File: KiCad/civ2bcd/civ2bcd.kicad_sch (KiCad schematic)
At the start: 56 parts, among them J1 7-15VDC, J2 CI-V (OUT), J3 SWD, J4 BCD OUTPUT 1, J5 BCD OUTPUT 2, J6 CI-V (IN), Q1 BC817, Q2 BC817, Q3 BC817, Q4 BC817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

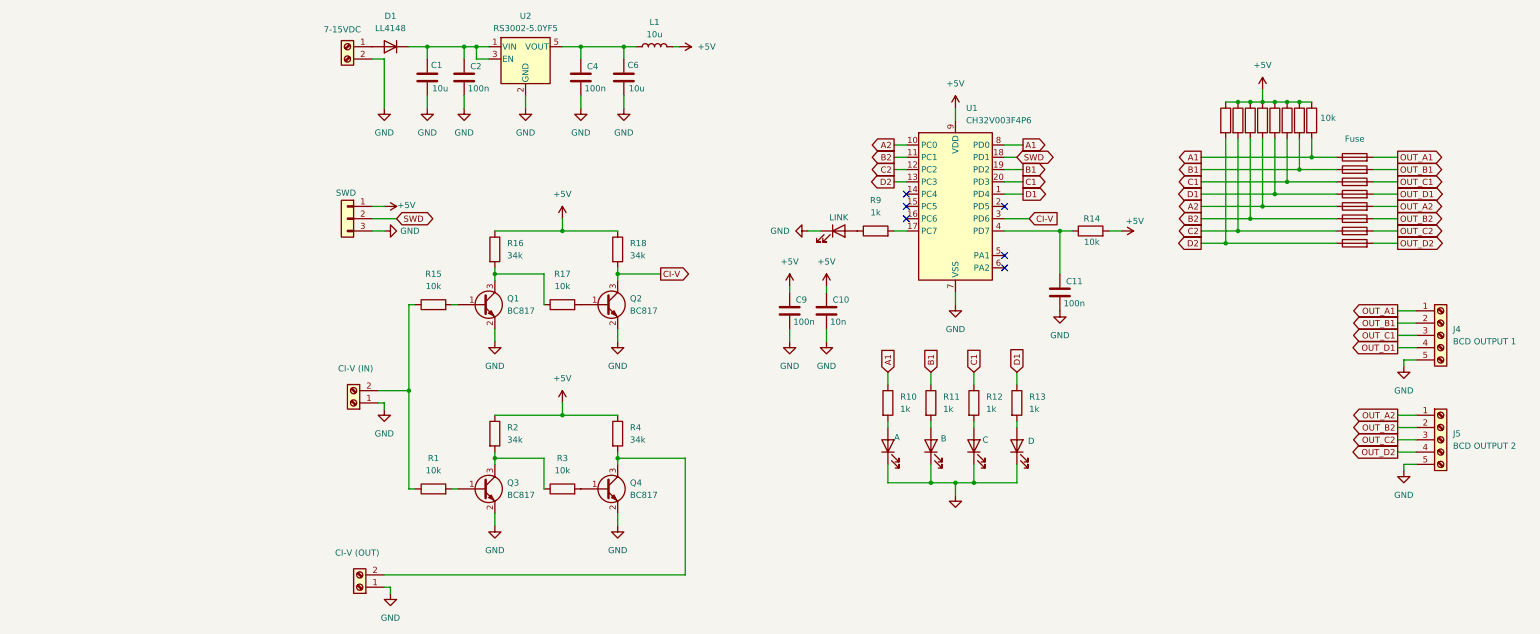
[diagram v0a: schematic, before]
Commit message: fix issues with civ input
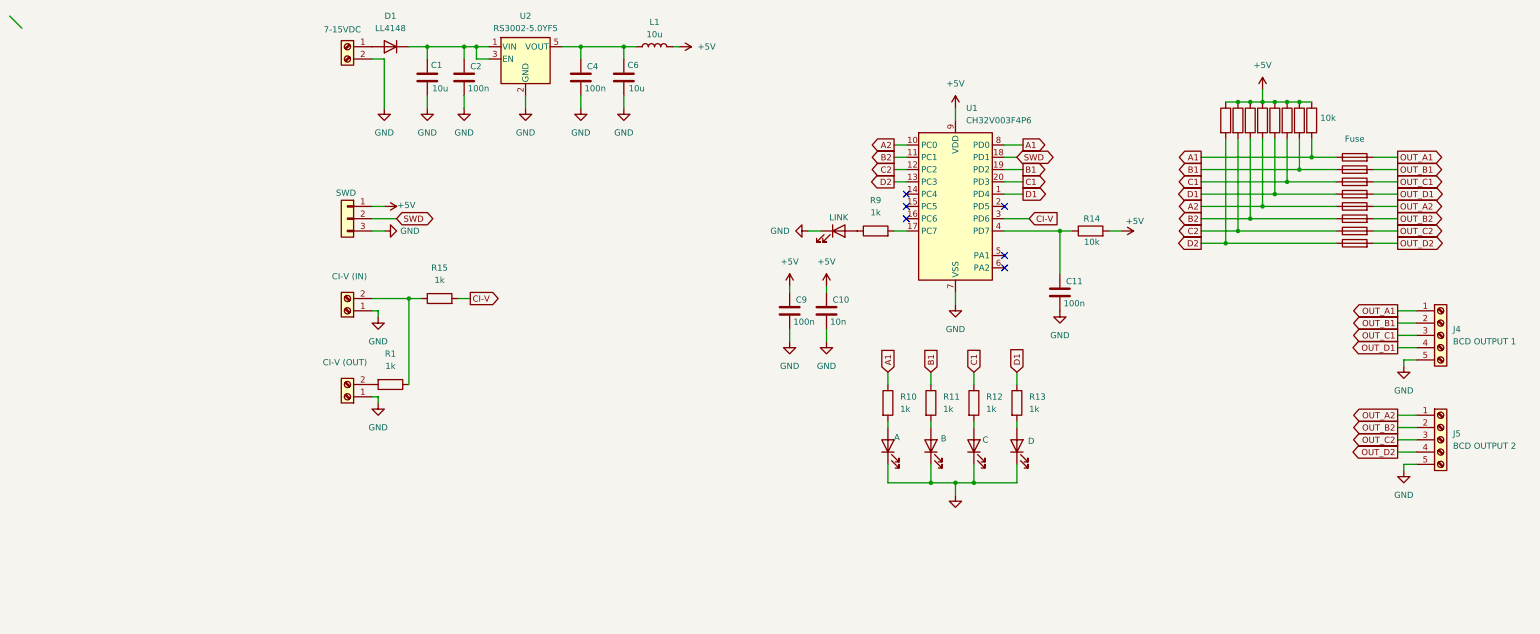
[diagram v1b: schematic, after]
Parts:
- removed Q1, Q2, Q3, Q4: BC817, Package_TO_SOT_SMD:SOT-23, symbol Transistor_BJT:BC817
- removed R16, R18, R2, R4: 34k, Resistor_SMD:R_1206_3216Metric, symbol Device:R
- removed R17, R3: 10k, Resistor_SMD:R_1206_3216Metric, symbol Device:R
- R1, R15: value 10k -> 1k
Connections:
- net CI-V: now also R15.2
- net at J2.2 (Pin_2): now also R1.2
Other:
- moved on the sheet: R1, R15

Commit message: fix civ connection
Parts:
- removed R1: 1k, Resistor_SMD:R_1206_3216Metric, symbol Device:R
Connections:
- net at J6.2 (Pin_2), R15.1: now also J2.2 (Pin_2)
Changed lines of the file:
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@@
 	(wire
 		(pts
+			(xy 34.29 104.14) (xy 41.91 104.14)
+		)
+		(stroke
+			(width 0)
+			(type default)
+		)
+	)
+	(wire
+		(pts
 			(xy 205.74 64.77) (xy 220.98 64.77)
 		)
@@
 					(unit 1)
 				)
-			)
-		)
-	)
-	(symbol
-		(lib_id "Device:R")
-		(at 38.1 104.14 270)
-		(unit 1)
-		(exclude_from_sim no)
-		(in_bom yes)
-		(on_board yes)
-		(dnp no)
-		(fields_autoplaced yes)
-		(property "Reference" "R1"
-			(at 38.1 97.79 90)
-			(effects
-				(font
-					(size 1.27 1.27)
-				)
-			)
-		)
-		(property "Value" "1k"
-			(at 38.1 100.33 90)
-			(effects
-				(font
-					(size 1.27 1.27)
-				)
-			)
-		)
-		(property "Footprint" "Resistor_SMD:R_1206_3216Metric"
-			(at 38.1 102.362 90)
-			(effects
-				(font
-					(size 1.27 1.27)
-				)
-				(hide yes)
-			)
-		)
-		(property "Datasheet" "~"
-			(at 38.1 104.14 0)
-			(effects
-				(font
-					(size 1.27 1.27)
-				)
-				(hide yes)
-			)
-		)
-		(property "Description" "Resistor"
-			(at 38.1 104.14 0)
-			(effects
-				(font
-					(size 1.27 1.27)
-				)
-				(hide yes)
-			)
-		)
-		(pin "2"
-		)
-		(pin "1"
-		)
-		(instances
-			(project "civ2bcd"
-				(path "/b6b947b0-072e-44b3-ada7-f9aaf0a4a828"
-					(reference "R1")
-					(unit 1)
-				)
